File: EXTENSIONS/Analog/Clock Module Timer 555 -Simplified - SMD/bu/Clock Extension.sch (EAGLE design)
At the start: 9 parts, among them T555_CLOCK NE555N, X1 USB-A

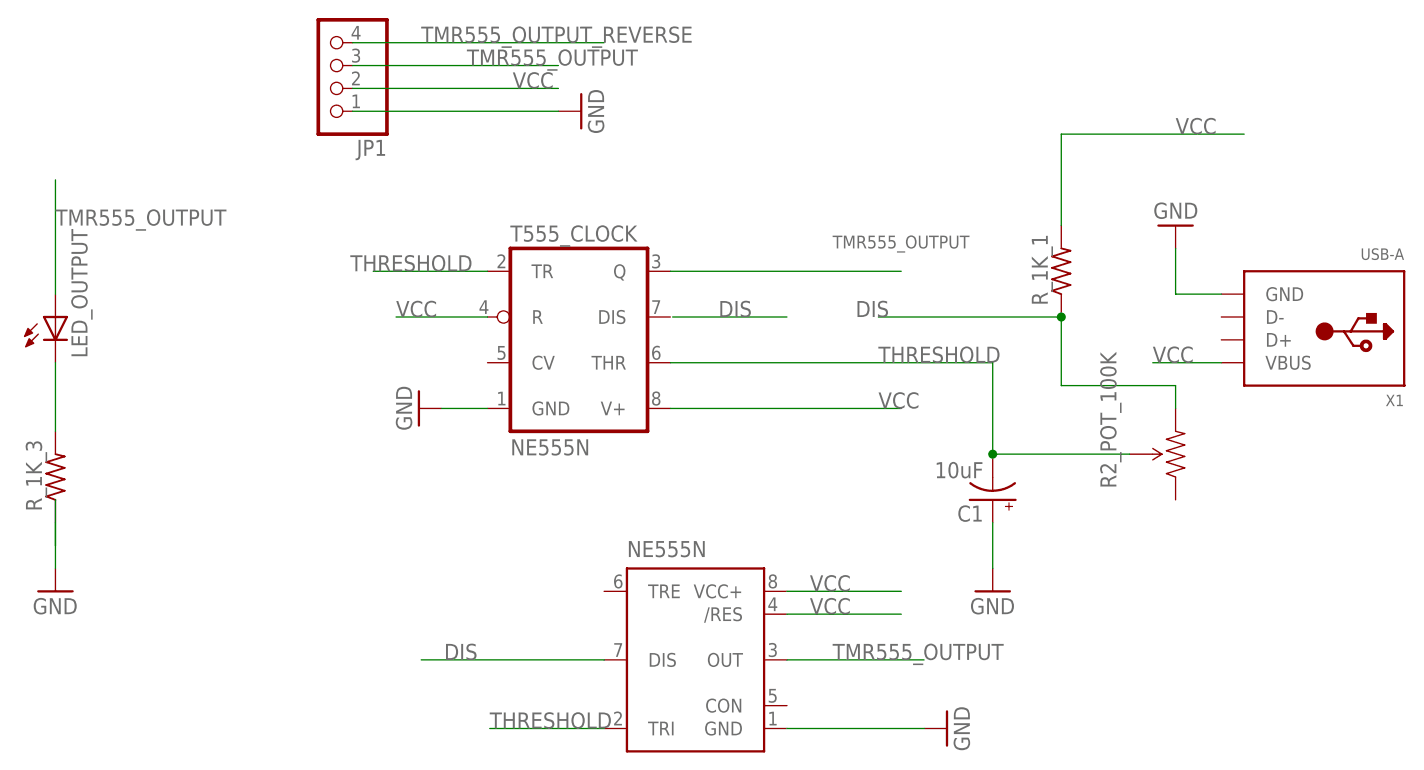
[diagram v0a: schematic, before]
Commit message: Create new clock module SMD
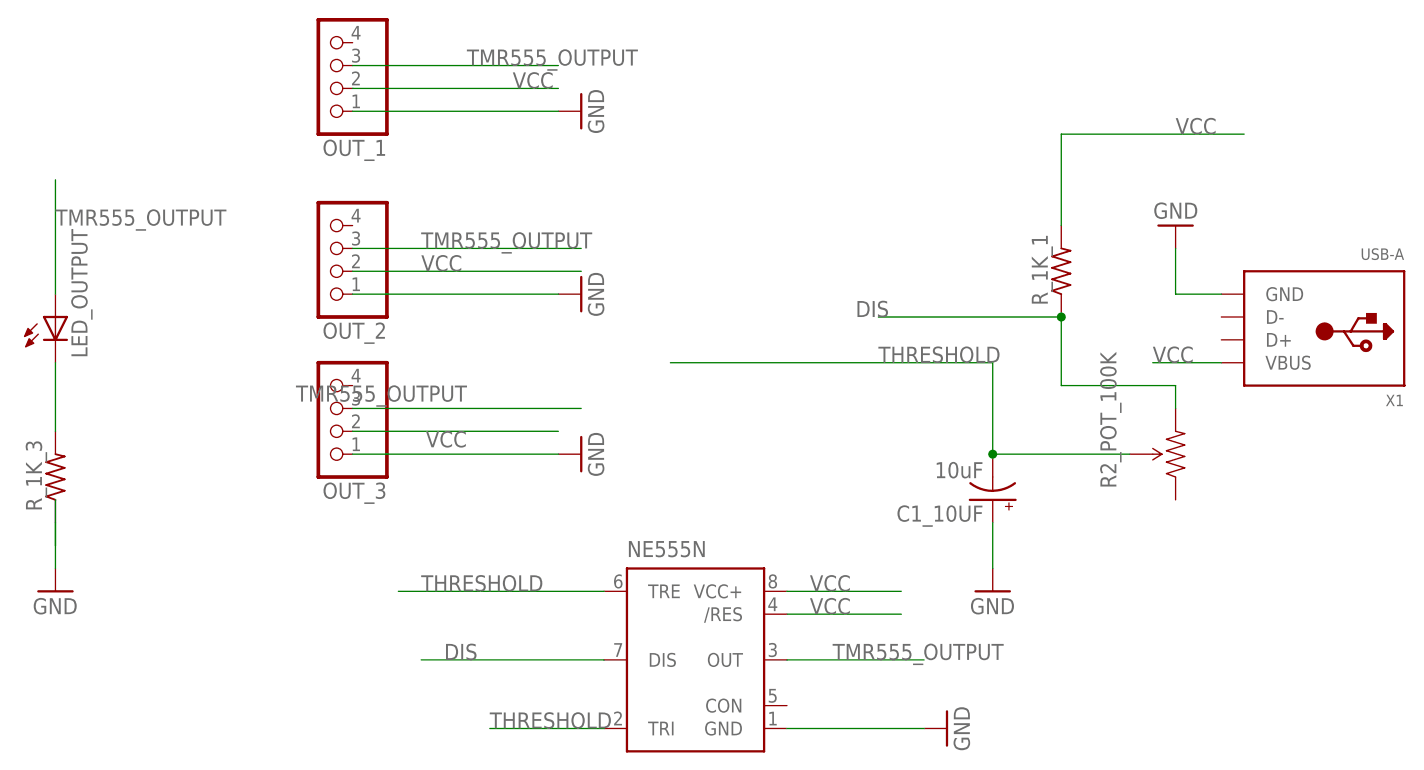
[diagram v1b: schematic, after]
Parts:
- removed T555_CLOCK: NE555N, linear:NE555N
- added OUT_2, OUT_3: (no value), pinhead:PINHD-1X4
- renumbered C1 to C1_10UF, JP1 to OUT_1
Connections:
- removed net TMR555_OUTPUT_REVERSE: OUT_1.4
- net GND: now also OUT_2.1, OUT_3.1; no longer T555_CLOCK.GND
- net THRESHOLD: now also NE555N.TRE; no longer T555_CLOCK.THR, T555_CLOCK.TR
- net TMR555_OUTPUT: now also OUT_2.3, OUT_3.3; no longer T555_CLOCK.Q
- net VCC: now also OUT_2.2, OUT_3.2; no longer T555_CLOCK.R, T555_CLOCK.V+
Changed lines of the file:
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@@
 <part name="X1" library="adafruit" deviceset="USB-A" device=""/>
 <part name="GND1" library="supply1" deviceset="GND" device=""/>
-<part name="T555_CLOCK" library="linear" deviceset="*555" device="N" technology="NE"/>
-<part name="GND2" library="supply1" deviceset="GND" device=""/>
 <part name="GND4" library="supply1" deviceset="GND" device=""/>
-<part name="JP1" library="pinhead" deviceset="PINHD-1X4" device=""/>
+<part name="OUT_1" library="pinhead" deviceset="PINHD-1X4" device=""/>
 <part name="GND5" library="supply1" deviceset="GND" device=""/>
 <part name="R_1K_1" library="adafruit" deviceset="R-US_" device="R1206"/>
@@
 <part name="R_1K_3" library="adafruit" deviceset="R-US_" device="R1206"/>
 <part name="GND7" library="supply1" deviceset="GND" device=""/>
-<part name="C1" library="SparkFun-Capacitors" deviceset="10UF-16V-10%(TANT)" device="" value="10uF"/>
+<part name="C1_10UF" library="SparkFun-Capacitors" deviceset="10UF-16V-10%(TANT)" device="" value="10uF"/>
 <part name="NE555N" library="SparkFun-AnalogIC" deviceset="NE555" device="D"/>
 <part name="GND3" library="supply1" deviceset="GND" device=""/>
+<part name="OUT_2" library="pinhead" deviceset="PINHD-1X4" device=""/>
+<part name="GND2" library="supply1" deviceset="GND" device=""/>
+<part name="OUT_3" library="pinhead" deviceset="PINHD-1X4" device=""/>
+<part name="GND6" library="supply1" deviceset="GND" device=""/>
 </parts>
 <sheets>
@@
 <instance part="X1" gate="G$1" x="127" y="99.06" rot="R180"/>
 <instance part="GND1" gate="1" x="111.76" y="109.22" rot="R180"/>
-<instance part="T555_CLOCK" gate="A" x="45.466" y="96.52"/>
-<instance part="GND2" gate="1" x="27.686" y="88.9" rot="R270"/>
 <instance part="GND4" gate="1" x="91.44" y="68.58"/>
-<instance part="JP1" gate="A" x="17.78" y="127" rot="R180"/>
+<instance part="OUT_1" gate="A" x="17.78" y="127" rot="R180"/>
 <instance part="GND5" gate="1" x="45.72" y="121.92" rot="R90"/>
 <instance part="R_1K_1" gate="G$1" x="99.06" y="104.14" rot="R90"/>
@@
 <instance part="R_1K_3" gate="G$1" x="-12.7" y="81.28" rot="R90"/>
 <instance part="GND7" gate="1" x="-12.7" y="68.58"/>
-<instance part="C1" gate="G$1" x="91.44" y="78.74" rot="R180"/>
+<instance part="C1_10UF" gate="G$1" x="91.44" y="78.74" rot="R180"/>
 <instance part="NE555N" gate="G$1" x="58.42" y="60.96"/>
 <instance part="GND3" gate="1" x="86.36" y="53.34" rot="R90"/>
+<instance part="OUT_2" gate="A" x="17.78" y="106.68" rot="R180"/>
+<instance part="GND2" gate="1" x="45.72" y="101.6" rot="R90"/>
+<instance part="OUT_3" gate="A" x="17.78" y="88.9" rot="R180"/>
+<instance part="GND6" gate="1" x="45.72" y="83.82" rot="R90"/>
 </instances>
 <busses>
@@
 </segment>
 <segment>
-<pinref part="GND2" gate="1" pin="GND"/>
-<pinref part="T555_CLOCK" gate="A" pin="GND"/>
-<wire x1="30.226" y1="88.9" x2="35.306" y2="88.9" width="0.1524" layer="91"/>
+<pinref part="GND4" gate="1" pin="GND"/>
+<wire x1="91.44" y1="76.2" x2="91.44" y2="71.12" width="0.1524" layer="91"/>
+<pinref part="C1_10UF" gate="G$1" pin="+"/>
 </segment>
 <segment>
-<pinref part="GND4" gate="1" pin="GND"/>
-<wire x1="91.44" y1="76.2" x2="91.44" y2="71.12" width="0.1524" layer="91"/>
-<pinref part="C1" gate="G$1" pin="+"/>
-</segment>
-<segment>
-<pinref part="JP1" gate="A" pin="1"/>
+<pinref part="OUT_1" gate="A" pin="1"/>
 <pinref part="GND5" gate="1" pin="GND"/>
 <wire x1="20.32" y1="121.92" x2="43.18" y2="121.92" width="0.1524" layer="91"/>
@@
 <wire x1="68.58" y1="53.34" x2="83.82" y2="53.34" width="0.1524" layer="91"/>
 </segment>
+<segment>
+<pinref part="OUT_2" gate="A" pin="1"/>
+<pinref part="GND2" gate="1" pin="GND"/>
+<wire x1="20.32" y1="101.6" x2="43.18" y2="101.6" width="0.1524" layer="91"/>
+</segment>
+<segment>
+<pinref part="OUT_3" gate="A" pin="1"/>
+<pinref part="GND6" gate="1" pin="GND"/>
+<wire x1="20.32" y1="83.82" x2="43.18" y2="83.82" width="0.1524" layer="91"/>
+</segment>
 </net>
 <net name="VCC" class="0">
@@
 </segment>
 <segment>
-<pinref part="T555_CLOCK" gate="A" pin="V+"/>
-<wire x1="55.626" y1="88.9" x2="81.28" y2="88.9" width="0.1524" layer="91"/>
-<label x="78.74" y="88.9" size="1.778" layer="95"/>
-</segment>
-<segment>
-<pinref part="T555_CLOCK" gate="A" pin="R"/>
-<wire x1="35.306" y1="99.06" x2="25.146" y2="99.06" width="0.1524" layer="91"/>
-<label x="25.146" y="99.06" size="1.778" layer="95"/>
-</segment>
-<segment>
-<pinref part="JP1" gate="A" pin="2"/>
+<pinref part="OUT_1" gate="A" pin="2"/>
 <wire x1="20.32" y1="124.46" x2="43.18" y2="124.46" width="0.1524" layer="91"/>
 <label x="38.1" y="124.46" size="1.778" layer="95"/>
@@
 <label x="71.12" y="68.58" size="1.778" layer="95"/>
 </segment>
+<segment>
+<pinref part="OUT_2" gate="A" pin="2"/>
+<wire x1="20.32" y1="104.14" x2="45.72" y2="104.14" width="0.1524" layer="91"/>
+<label x="27.94" y="104.14" size="1.778" layer="95"/>
+</segment>
+<segment>
+<pinref part="OUT_3" gate="A" pin="2"/>
+<wire x1="20.32" y1="86.36" x2="43.18" y2="86.36" width="0.1524" layer="91"/>
+<label x="33.02" y="86.36" size="1.778" layer="95" rot="R180"/>
+</segment>
 </net>
 <net name="THRESHOLD" class="0">
 <segment>
-<pinref part="T555_CLOCK" gate="A" pin="THR"/>
 <wire x1="55.626" y1="93.98" x2="91.44" y2="93.98" width="0.1524" layer="91"/>
 <label x="78.74" y="93.98" size="1.778" layer="95"/>
@@
 <pinref part="R2_POT_100K" gate="R?" pin="WIPER"/>
 <wire x1="106.68" y1="83.82" x2="91.44" y2="83.82" width="0.1524" layer="91"/>
-<pinref part="C1" gate="G$1" pin="-"/>
+<pinref part="C1_10UF" gate="G$1" pin="-"/>
 <junction x="91.44" y="83.82"/>
-</segment>
-<segment>
-<pinref part="T555_CLOCK" gate="A" pin="TR"/>
-<wire x1="35.306" y1="104.14" x2="22.606" y2="104.14" width="0.1524" layer="91"/>
-<label x="20.066" y="104.14" size="1.778" layer="95"/>
 </segment>
 <segment>
@@
 <label x="35.56" y="53.34" size="1.778" layer="95"/>
 </segment>
+<segment>
+<pinref part="NE555N" gate="G$1" pin="TRE"/>
+<wire x1="48.26" y1="68.58" x2="25.4" y2="68.58" width="0.1524" layer="91"/>
+<label x="27.94" y="68.58" size="1.778" layer="95"/>
+</segment>
 </net>
 <net name="TMR555_OUTPUT" class="0">
 <segment>
-<pinref part="T555_CLOCK" gate="A" pin="Q"/>
-<wire x1="55.626" y1="104.14" x2="81.28" y2="104.14" width="0.1524" layer="91"/>
-<label x="73.66" y="106.68" size="1.4224" layer="95"/>
-</segment>
-<segment>
-<pinref part="JP1" gate="A" pin="3"/>
+<pinref part="OUT_1" gate="A" pin="3"/>
 <wire x1="20.32" y1="127" x2="43.18" y2="127" width="0.1524" layer="91"/>
 <label x="33.02" y="127" size="1.778" layer="95"/>
@@
 <label x="73.66" y="60.96" size="1.778" layer="95"/>
 </segment>
+<segment>
+<pinref part="OUT_2" gate="A" pin="3"/>
+<wire x1="20.32" y1="106.68" x2="45.72" y2="106.68" width="0.1524" layer="91"/>
+<label x="27.94" y="106.68" size="1.778" layer="95"/>
+</segment>
+<segment>
+<pinref part="OUT_3" gate="A" pin="3"/>
+<wire x1="20.32" y1="88.9" x2="45.72" y2="88.9" width="0.1524" layer="91"/>
+<label x="33.02" y="91.44" size="1.778" layer="95" rot="R180"/>
+</segment>
 </net>
 <net name="N$5" class="0">
@@
 </segment>
 </net>
-<net name="TMR555_OUTPUT_REVERSE" class="0">
-<segment>
-<pinref part="JP1" gate="A" pin="4"/>
-<wire x1="20.32" y1="129.54" x2="48.26" y2="129.54" width="0.1524" layer="91"/>
-<label x="27.94" y="129.54" size="1.778" layer="95"/>
-</segment>
-</net>
 <net name="DIS" class="0">
 <segment>
-<wire x1="55.88" y1="99.06" x2="68.58" y2="99.06" width="0.1524" layer="91"/>
-<label x="60.96" y="99.06" size="1.778" layer="95"/>
-</segment>
-<segment>
 <pinref part="R_1K_1" gate="G$1" pin="1"/>
